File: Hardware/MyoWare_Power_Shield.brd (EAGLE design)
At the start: 52.1 x 20.7 mm, 16 parts

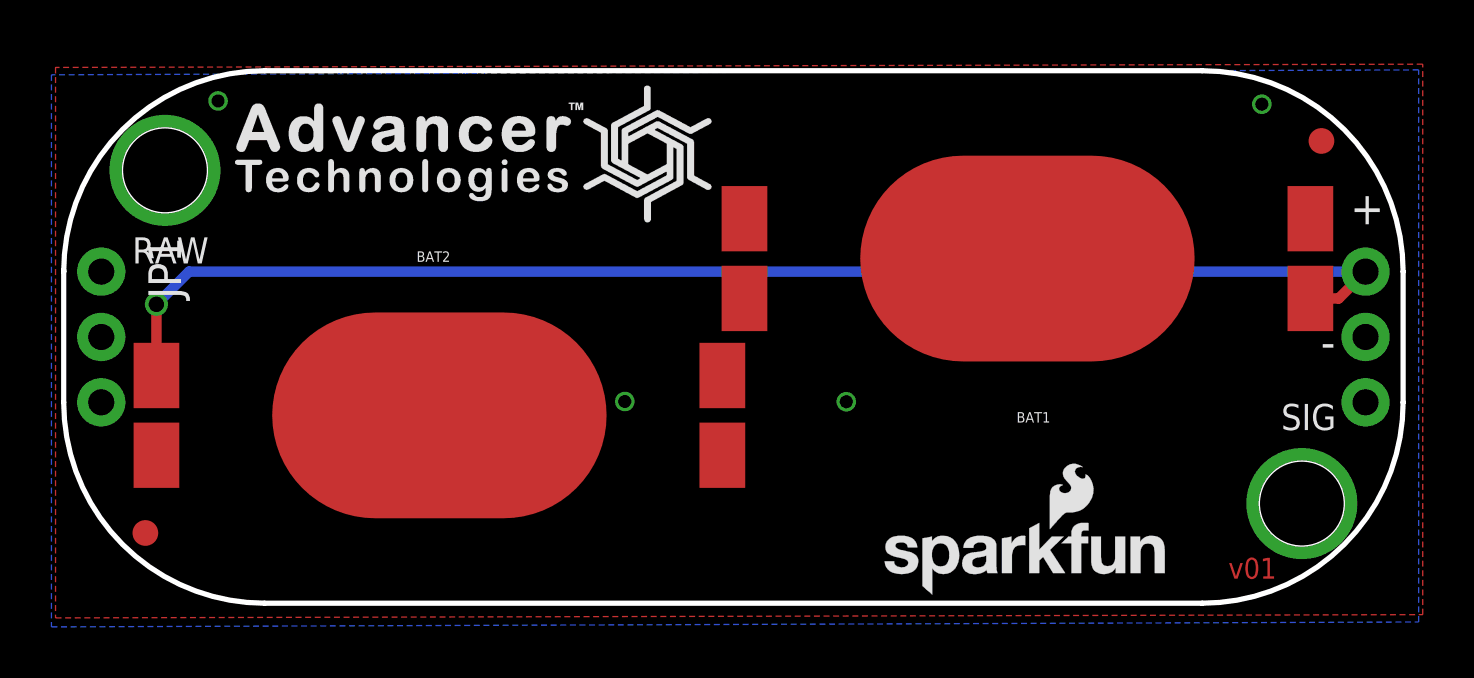
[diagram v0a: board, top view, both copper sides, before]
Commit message: Changed to standard paste version of battery holder
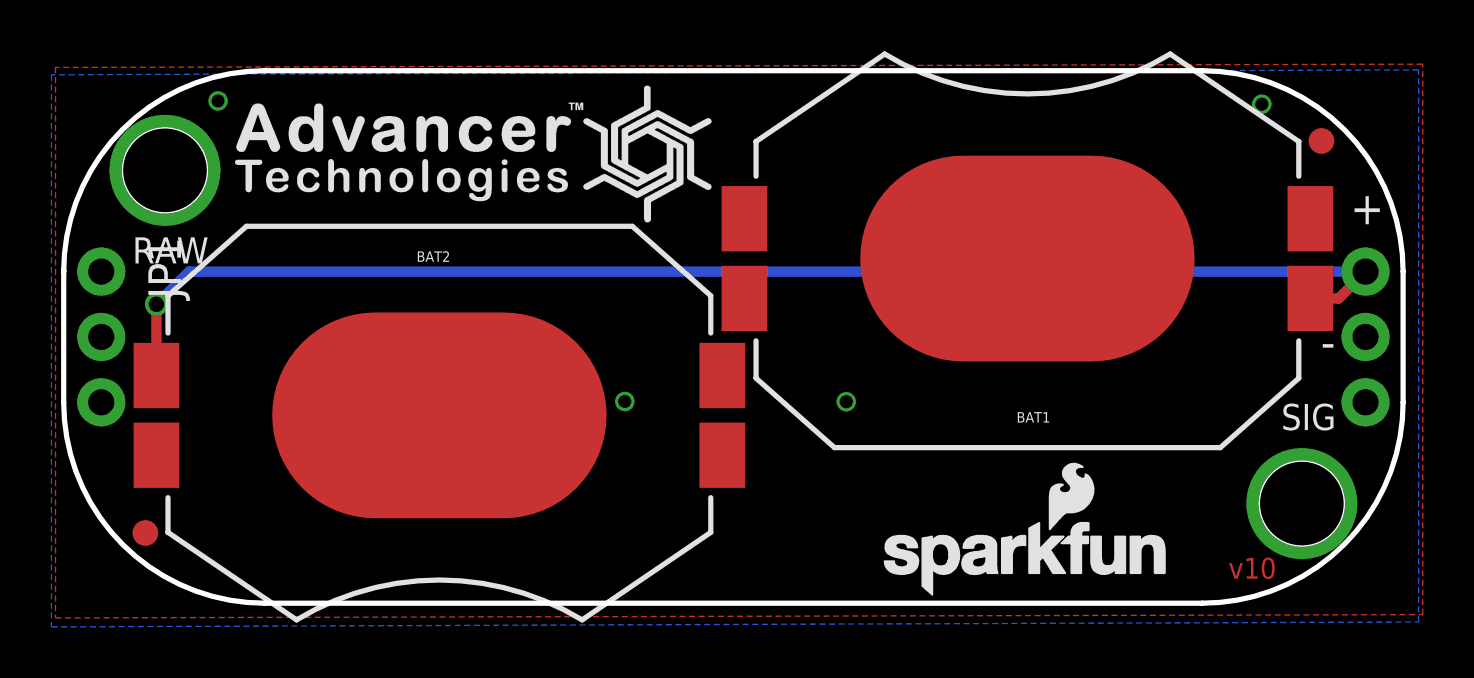
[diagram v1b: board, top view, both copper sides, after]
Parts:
- BAT1, BAT2: value (none) -> 20mm coincell; device SparkFun-Electromechanical:BATTCON_20MM_4LEGS_OVERPASTE -> SparkFun-Electromechanical:BATTCON_20MM_4LEGS
- U$3: device advancer-technologies:ROHS -> SparkFun-Aesthetics:ROHS_LOGO_0.18_IN
- U$5: device advancer-technologies:PB-FREE -> SparkFun-Aesthetics:NO_PB_LOGO_0.120
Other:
- board text added: "v10"
- board text removed: "v01"
